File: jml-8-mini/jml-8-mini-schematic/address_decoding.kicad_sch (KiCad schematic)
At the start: 4 parts, among them U6 74LS04, U7 74154, U8 74LS139, U9 74LS08

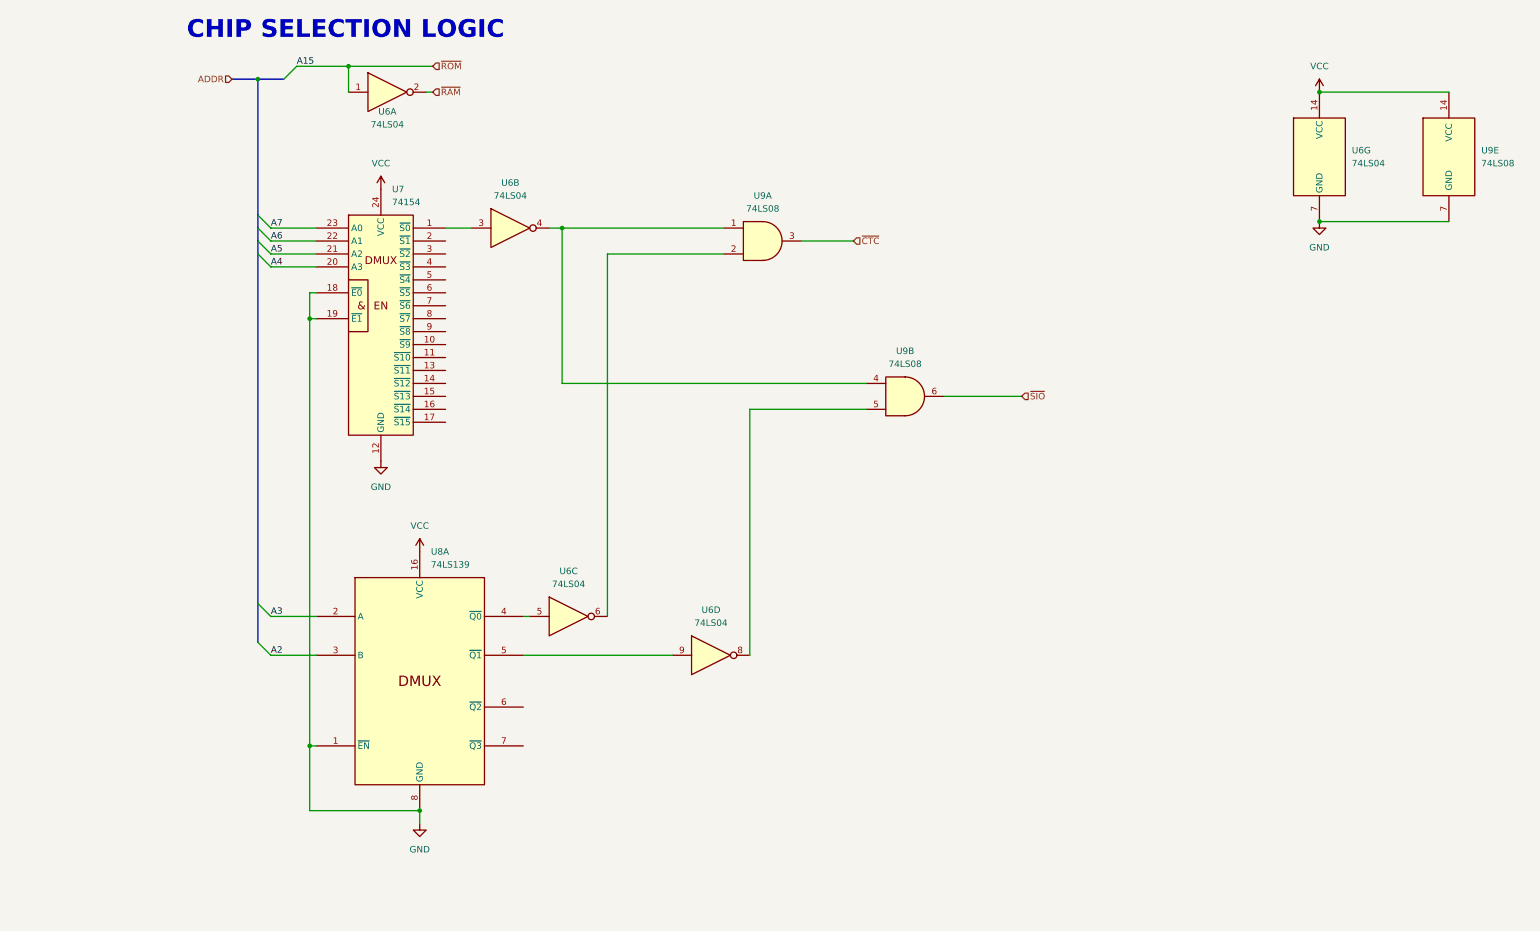
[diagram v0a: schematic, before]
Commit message: update schematic, new program to test RAM
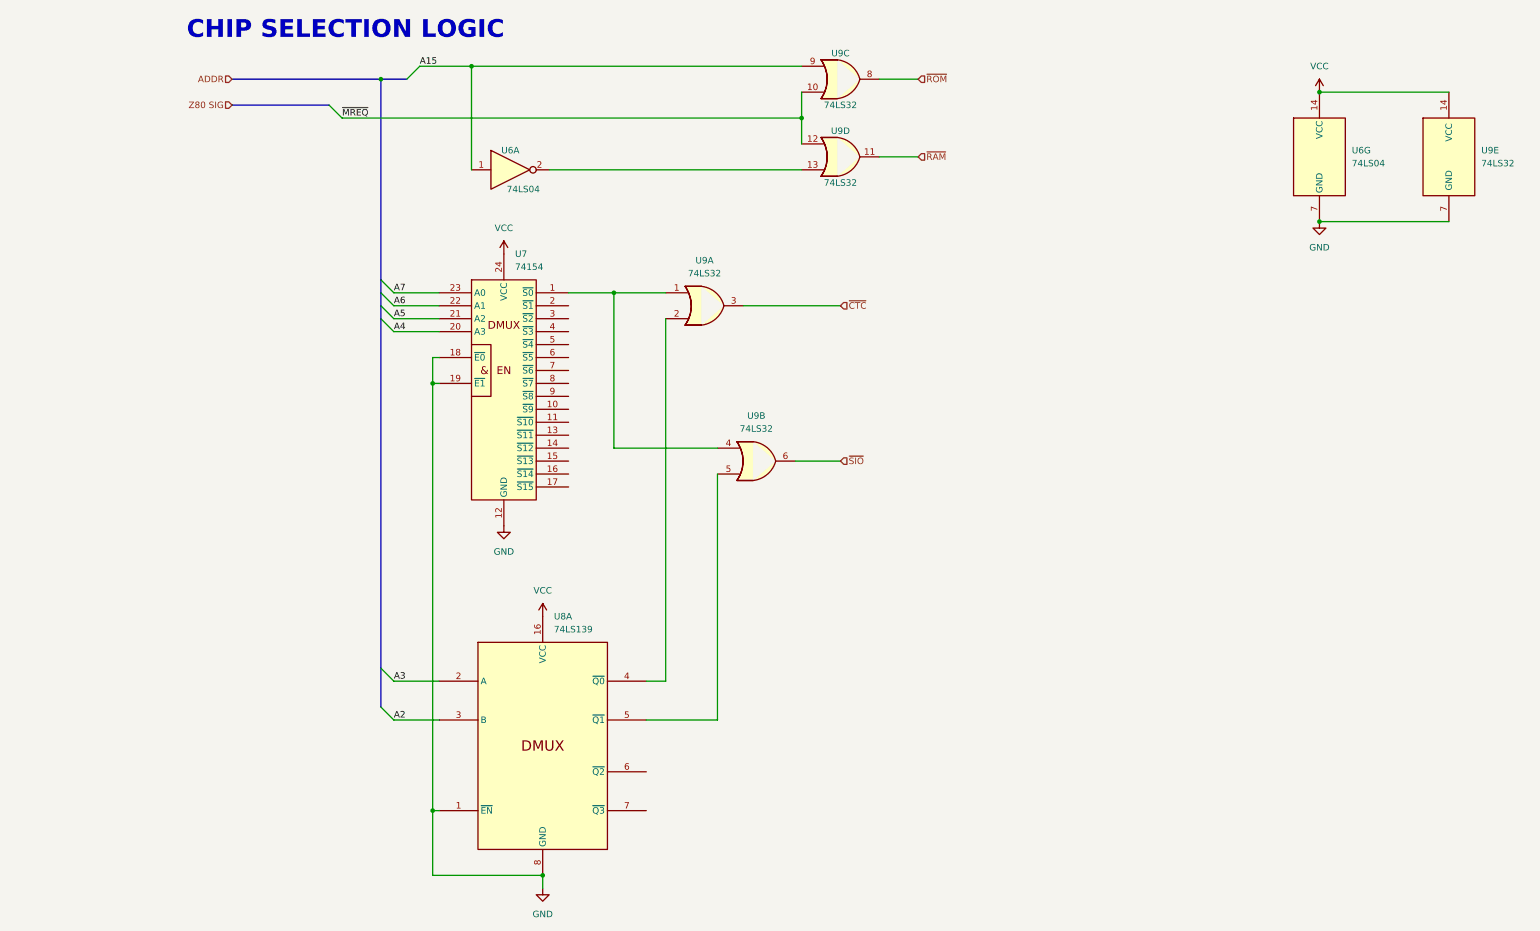
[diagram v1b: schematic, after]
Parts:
- removed unit 4 of U6
- removed unit 3 of U6
- removed unit 2 of U6
- removed U9: 74LS08, symbol 74xx:74LS08
- added U9: 74LS32, symbol 74xx:74LS32
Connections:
- net GND: now also U9.7 (GND)
- net VCC: now also U9.14 (VCC)
- net ~{CTC}: now also U9.3
- net ~{RAM}: now also U9.11; no longer U6.2
- net ~{ROM}: now also U9.8; no longer U6.1
- net ~{SIO}: now also U9.6
- net at U7.1 (~{S0}): now also U9.1, U9.4
- net at U8.5 (~{Q1}): now also U9.5
- net at U8.4 (~{Q0}): now also U9.2
- new net: U6.2, U9.13
- new net A15: U6.1, U9.9
- new net ~{MREQ}: U9.10, U9.12
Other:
- moved on the sheet: U6A, U7, U8A

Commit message: updates to jml-8 mini schematic
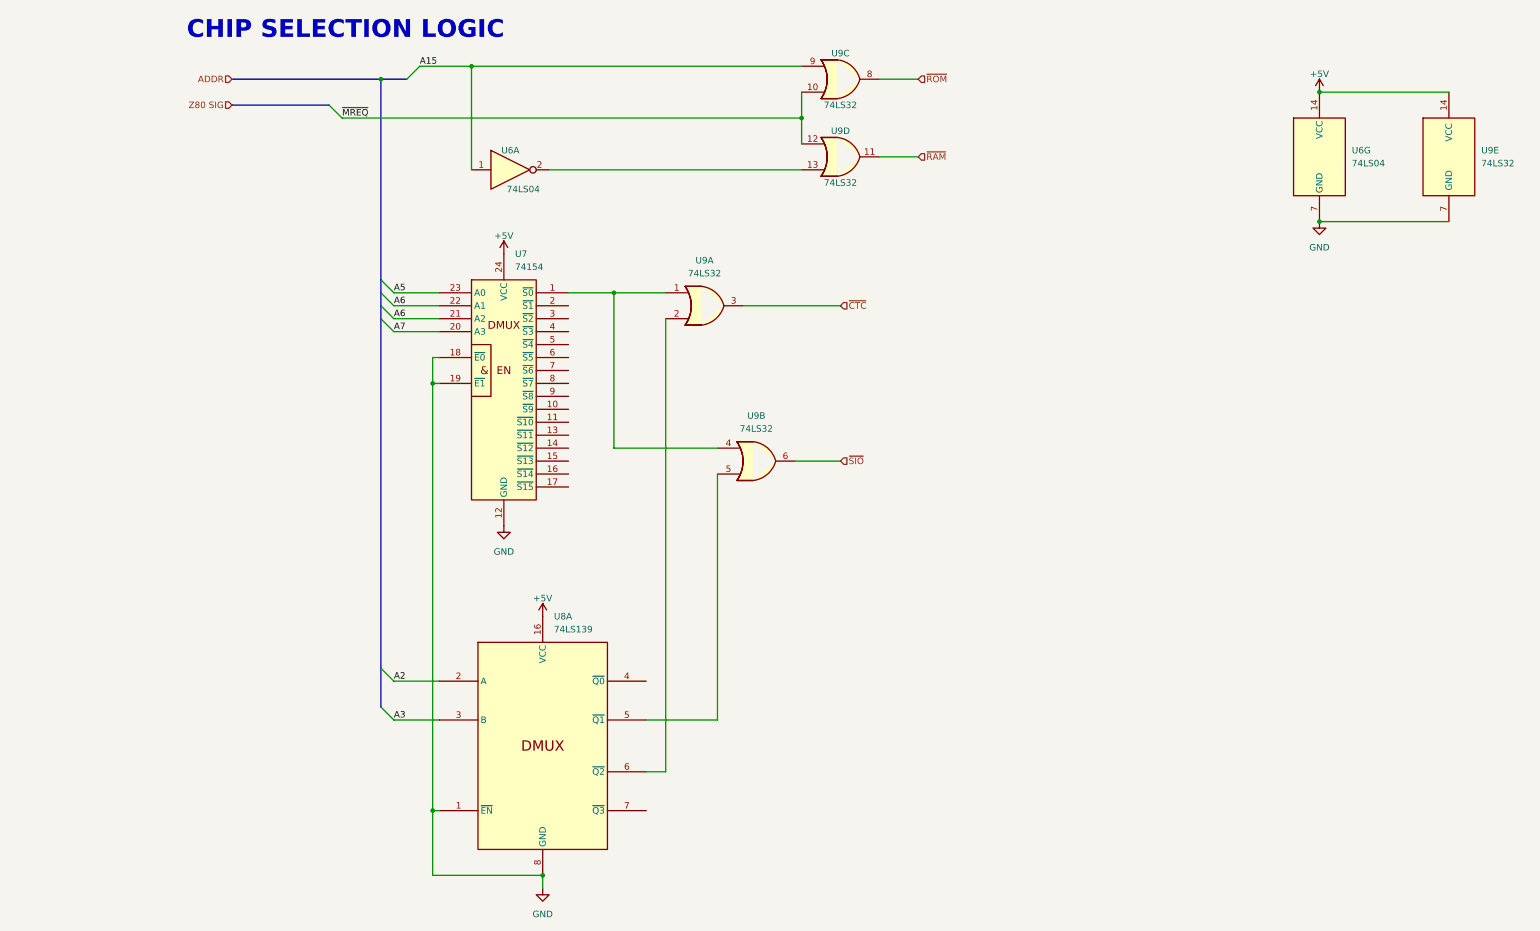
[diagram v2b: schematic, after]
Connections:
- net A4 is gone; now on net A7: U7.20 (A3)
- net A2: now also U8.2 (A); no longer U8.3 (B)
- net A3: now also U8.3 (B); no longer U8.2 (A)
- net A5: now also U7.23 (A0); no longer U7.21 (A2)
- net A6: now also U7.21 (A2)
- net A7: no longer U7.23 (A0)
- net at U9.2: now also U8.6 (~{Q2}); no longer U8.4 (~{Q0})
- net VCC renamed +5V
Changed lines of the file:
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@@
-    (stroke (width 0) (type default))
-  )
-  (wire (pts (xy 109.22 147.32) (xy 109.22 76.2))
     (stroke (width 0) (type default))
   )
@@
     (stroke (width 0) (type default))
   )
-  (wire (pts (xy 105.41 147.32) (xy 109.22 147.32))
-    (stroke (width 0) (type default))
-  )
   (wire (pts (xy 55.88 71.12) (xy 64.77 71.12))
     (stroke (width 0) (type default))
@@
     (stroke (width 0) (type default))
   )
+  (wire (pts (xy 105.41 165.1) (xy 109.22 165.1))
+    (stroke (width 0) (type default))
+  )
   (bus (pts (xy 53.34 71.12) (xy 53.34 73.66))
     (stroke (width 0) (type default))
   )
   (wire (pts (xy 63.5 88.9) (xy 64.77 88.9))
+    (stroke (width 0) (type default))
+  )
+  (wire (pts (xy 109.22 76.2) (xy 109.22 165.1))
     (stroke (width 0) (type default))
   )
@@
     (effects (font (size 3.5 3.5) bold) (justify left bottom))
   )
-  (label "A2" (at 55.88 154.94 0) (fields_autoplaced)
+  (label "A3" (at 55.88 154.94 0) (fields_autoplaced)
     (effects (font (size 1.27 1.27)) (justify left bottom))
   )
@@
     (effects (font (size 1.27 1.27)) (justify left bottom))
   )
-  (label "A7" (at 55.88 71.12 0) (fields_autoplaced)
-    (effects (font (size 1.27 1.27)) (justify left bottom))
-  )
-  (label "A5" (at 55.88 76.2 0) (fields_autoplaced)
+  (label "A5" (at 55.88 71.12 0) (fields_autoplaced)
+    (effects (font (size 1.27 1.27)) (justify left bottom))
+  )
+  (label "A6" (at 55.88 76.2 0) (fields_autoplaced)
     (effects (font (size 1.27 1.27)) (justify left bottom))
   )
@@
     (effects (font (size 1.27 1.27)) (justify left bottom))
   )
-  (label "A4" (at 55.88 78.74 0) (fields_autoplaced)
+  (label "A7" (at 55.88 78.74 0) (fields_autoplaced)
     (effects (font (size 1.27 1.27)) (justify left bottom))
   )
@@
     (effects (font (size 1.27 1.27)) (justify left bottom))
   )
-  (label "A3" (at 55.88 147.32 0) (fields_autoplaced)
+  (label "A2" (at 55.88 147.32 0) (fields_autoplaced)
     (effects (font (size 1.27 1.27)) (justify left bottom))
   )
@@
     )
   )
-  (symbol (lib_id "power:VCC") (at 237.49 31.75 0) (unit 1)
+  (symbol (lib_id "power:+5V") (at 237.49 31.75 0) (unit 1)
     (in_bom yes) (on_board yes) (dnp no) (fields_autoplaced)
     (property "Reference" "#PWR015" (at 237.49 35.56 0)
       (effects (font (size 1.27 1.27)) hide)
     )
-    (property "Value" "VCC" (at 237.49 26.67 0)
+    (property "Value" "+5V" (at 237.49 28.194 0)
       (effects (font (size 1.27 1.27)))
     )
@@
         )
         (path "/7f93abb4-2372-4a9e-a664-5edb67349db4/0d9b5471-55ed-4c8b-801f-ea410459ca65"
-          (reference "#PWR015") (unit 1)
+          (reference "#PWR?") (unit 1)
         )
       )
@@
     )
   )
-  (symbol (lib_id "power:VCC") (at 77.47 63.5 0) (unit 1)
-    (in_bom yes) (on_board yes) (dnp no) (fields_autoplaced)
-    (property "Reference" "#PWR021" (at 77.47 67.31 0)
-      (effects (font (size 1.27 1.27)) hide)
-    )
-    (property "Value" "VCC" (at 77.47 58.42 0)
+  (symbol (lib_id "power:+5V") (at 77.47 63.5 0) (unit 1)
+    (in_bom yes) (on_board yes) (dnp no) (fields_autoplaced)
+    (property "Reference" "#PWR?" (at 77.47 67.31 0)
+      (effects (font (size 1.27 1.27)) hide)
+    )
+    (property "Value" "+5V" (at 77.47 59.944 0)
       (effects (font (size 1.27 1.27)))
     )
@@
       (project "jml-8-mini"
         (path "/7f93abb4-2372-4a9e-a664-5edb67349db4/0d9b5471-55ed-4c8b-801f-ea410459ca65"
-          (reference "#PWR021") (unit 1)
+          (reference "#PWR?") (unit 1)
         )
       )
@@
     )
   )
-  (symbol (lib_id "power:VCC") (at 85.09 134.62 0) (unit 1)
-    (in_bom yes) (on_board yes) (dnp no) (fields_autoplaced)
-    (property "Reference" "#PWR020" (at 85.09 138.43 0)
-      (effects (font (size 1.27 1.27)) hide)
-    )
-    (property "Value" "VCC" (at 85.09 129.54 0)
+  (symbol (lib_id "power:+5V") (at 85.09 134.62 0) (unit 1)
+    (in_bom yes) (on_board yes) (dnp no) (fields_autoplaced)
+    (property "Reference" "#PWR?" (at 85.09 138.43 0)
+      (effects (font (size 1.27 1.27)) hide)
+    )
+    (property "Value" "+5V" (at 85.09 131.064 0)
       (effects (font (size 1.27 1.27)))
     )
@@
       (project "jml-8-mini"
         (path "/7f93abb4-2372-4a9e-a664-5edb67349db4/0d9b5471-55ed-4c8b-801f-ea410459ca65"
-          (reference "#PWR020") (unit 1)
-        )
-      )
+          (reference "#PWR?") (unit 1)
+        )
+      )

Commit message: updates to schematics
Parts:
- removed U7: 74154, symbol 74xx_IEEE:74154
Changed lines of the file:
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@@
-    )
-  )
-  (symbol (lib_id "74xx_IEEE:74154") (at 77.47 91.44 0) (unit 1)
-    (in_bom yes) (on_board yes) (dnp no) (fields_autoplaced)
-    (property "Reference" "U7" (at 79.6641 63.5 0)
-      (effects (font (size 1.27 1.27)) (justify left))
-    )
-    (property "Value" "74154" (at 79.6641 66.04 0)
-      (effects (font (size 1.27 1.27)) (justify left))
-    )
-    (property "Footprint" "" (at 77.47 91.44 0)
-      (effects (font (size 1.27 1.27)) hide)
-    )
-    (property "Datasheet" "" (at 77.47 91.44 0)
-      (effects (font (size 1.27 1.27)) hide)
-    )
-    (pin "12")
-    (pin "24")
-    (pin "1")
-    (pin "10")
-    (pin "11")
-    (pin "13")
-    (pin "14")
-    (pin "15")
-    (pin "16")
-    (pin "17")
-    (pin "18")
-    (pin "19")
-    (pin "2")
-    (pin "20")
-    (pin "21")
-    (pin "22")
-    (pin "23")
-    (pin "3")
-    (pin "4")
-    (pin "5")
-    (pin "6")
-    (pin "7")
-    (pin "8")
-    (pin "9")
-    (instances
-      (project "jml-8-mini"
-        (path "/7f93abb4-2372-4a9e-a664-5edb67349db4/0d9b5471-55ed-4c8b-801f-ea410459ca65"
-          (reference "U7") (unit 1)
-        )
-      )
     )
   )

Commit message: many changes to schematic to make more organized
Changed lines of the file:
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@@
 (kicad_sch (version 20230121) (generator eeschema)
   (paper "A4")
+  (title_block
+    (date "2023-09-22")
+    (rev "A")
+    (comment 1 "Author: Jacob Long")
+  )
   (junction (at 237.49 57.15) (diameter 0) (color 0 0 0 0)
   )
@@
     (stroke (width 0) (type default))
   )
-  (bus (pts (xy 24.13 29.21) (xy 53.34 29.21))
+  (bus (pts (xy 27.94 29.21) (xy 53.34 29.21))
     (stroke (width 0) (type default))
   )
@@
     (stroke (width 0) (type default))
   )
-  (bus (pts (xy 24.13 34.29) (xy 43.18 34.29))
+  (bus (pts (xy 27.94 34.29) (xy 43.18 34.29))
     (stroke (width 0) (type default))
   )
@@
     (effects (font (size 1.27 1.27)) (justify left))
   )
-  (hierarchical_label "Z80 SIG" (shape input) (at 24.13 34.29 180) (fields_autoplaced)
+  (hierarchical_label "Z80 SIG BUS" (shape input) (at 27.94 34.29 180) (fields_autoplaced)
     (effects (font (size 1.27 1.27)) (justify right))
   )
@@
     (effects (font (size 1.27 1.27)) (justify left))
   )
-  (hierarchical_label "ADDR" (shape input) (at 24.13 29.21 180) (fields_autoplaced)
+  (hierarchical_label "ADDR BUS" (shape input) (at 27.94 29.21 180) (fields_autoplaced)
     (effects (font (size 1.27 1.27)) (justify right))
   )
